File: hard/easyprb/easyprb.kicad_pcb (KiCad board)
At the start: 2 copper layers, 101 parts, among them J10 DBG, J20 RLTC, J21 CMD, J30 RS485, J40 TO EPF, J41 EPF, J50 TO RS, J51 UF RS485, Q30 S8050, Q40 2N7002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

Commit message: hardware is complete. it is does manufacture.
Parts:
- D51: value RED -> BLUE
- U30, U40, U50, U51: footprint Package_SO:SOIC-8_3.9x4.9mm_P1.27mm -> kicad_footprint_general:SOIC-8_3.9x4.9mm_P1.27mm
- U60, U61, U62, U63: footprint Package_SO:SOIC-8_5.23x5.23mm_P1.27mm -> kicad_footprint_general:SOIC-8_5.23x5.23mm_P1.27mm
- moved R32 85.3 mm to (116.8, 128.1), turned to 270 degrees
- moved R38 85.3 mm to (120.5, 137.9), turned to 90 degrees
- moved C27 80.9 mm to (112.6, 101.7), turned to 180 degrees
- moved C29 78.0 mm to (112.4, 113.7), turned to 180 degrees
- moved R30 77.4 mm to (113.3, 130.3), turned to 180 degrees
- moved J51 72.6 mm to (183.5, 136.4), turned to 90 degrees
- moved D23 72.5 mm to (116.3, 114.5), turned to 270 degrees
- moved C26 69.2 mm to (112.6, 100.2), turned to 180 degrees
- moved R21 67.6 mm to (114.7, 114.5), turned to 90 degrees
- moved C62 65.4 mm to (141.4, 135.2)
- moved J21 64.9 mm to (103.9, 110.3), turned to 90 degrees
- moved R13 64.9 mm to (127.5, 113.2)
- moved U30 64.1 mm to (121.9, 131.5), turned to 90 degrees
- moved D20 64.0 mm to (119.9, 84.5), turned to 180 degrees
- moved R34 63.8 mm to (116.8, 134.8), turned to 270 degrees
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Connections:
- J10 pad 1: /RST -> Net-(J10-Pad1)
- R37 pad 1: /LTX0 -> /LTX1
- U10 pad 11: /LE1 -> Net-(U10-Pad11)
- U10 pad 14: /LTX1 -> /EPN
- U10 pad 15: /LRX1 -> /EPN
- U10 pad 16: /TX1 -> /EPF
- U10 pad 18: /LE0 -> Net-(U10-Pad18)
- U10 pad 2: Net-(U10-Pad2) -> /TLL
- U10 pad 20: Net-(U10-Pad20) -> /TX1
- U10 pad 21: Net-(U10-Pad21) -> /LE0
- U10 pad 23: /LE2 -> Net-(U10-Pad23)
- U10 pad 24: /LTX0 -> Net-(U10-Pad24)
- U10 pad 25: /LRX0 -> Net-(U10-Pad25)
- U10 pad 26: /LRX0 -> Net-(U10-Pad26)
- U10 pad 27: /CFT -> Net-(U10-Pad27)
- U10 pad 28: Net-(U10-Pad28) -> /LEM
- U10 pad 30: Net-(U10-Pad30) -> /LRX0
- U10 pad 33: Net-(U10-Pad33) -> /LTX0
- U10 pad 34: /EPN -> Net-(U10-Pad34)
- U10 pad 35: /EPN -> /LE1
- U10 pad 36: Net-(U10-Pad36) -> /LE2
- U10 pad 37: /EPF -> /TEN
- U10 pad 38: /LE4 -> /CS3
- U10 pad 41: /LE3 -> Net-(U10-Pad41)
- U10 pad 42: /TX0 -> Net-(U10-Pad42)
- U10 pad 43: /RX0 -> Net-(U10-Pad43)
- U10 pad 44: /TLL -> Net-(U10-Pad44)
- U10 pad 46: Net-(U10-Pad46) -> /SWD
- U10 pad 47: /SWD -> /CS2
- U10 pad 48: Net-(U10-Pad48) -> /CS0
- U10 pad 51: /CS3 -> /LTX1
- U10 pad 52: /CS2 -> /LRX1
- U10 pad 53: /CS1 -> /LRX1
- U10 pad 54: /CS0 -> /CFT
- U10 pad 58: /LEM -> /CS1
- U10 pad 59: Net-(U10-Pad59) -> /LE3
- U10 pad 61: Net-(U10-Pad61) -> /TX0
- U10 pad 62: Net-(U10-Pad62) -> /RX0
- U10 pad 9: Net-(U10-Pad9) -> /LE4
- U22 pad 8: /LRX1 -> /LRX0
- U22 pad 9: /LTX1 -> /LTX0
- U30 pad 1: /LRX0 -> /LRX1
- U30 pad 4: /LTX0 -> /LTX1
- U31 pad 1: /LRX0 -> /LTX1
- U31 pad 2: /LTX0 -> /LRX1
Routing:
- net GND: track 0.00 -> 667.3 mm, vias 0 -> 85
- net VCC: track 0.00 -> 421.4 mm, vias 0 -> 23
- net /SCLK: track 0.00 -> 66.7 mm, vias 0 -> 5
- net /MOSI: track 0.00 -> 60.1 mm, vias 0 -> 4
- net /VUB: track 0.00 -> 55.8 mm, vias 0 -> 2
- net /MISO: track 0.00 -> 53.3 mm, vias 0 -> 6
- net /VUA: track 0.00 -> 46.9 mm, vias 0 -> 1
- net /LE3: track 0.00 -> 46.5 mm
- net /CS3: track 0.00 -> 43.4 mm, vias 0 -> 4
- net /LE2: track 0.00 -> 43.3 mm, vias 0 -> 2
- net /RX1: track 0.00 -> 39.1 mm
- net /LE0: track 0.00 -> 38.5 mm
- net /TX1: track 0.00 -> 38.4 mm, vias 0 -> 2
- net /TEN: track 0.00 -> 38.4 mm, vias 0 -> 2
- net /LRX1: track 0.00 -> 34.7 mm, vias 0 -> 2
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- added copper zone on B.Cu, net GND
- added copper zone on F.Cu, net GND
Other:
- board outline added: 87 x 72 mm
- net class Default: trace_width 0.25 -> 0.2; via_dia 0.8 -> 0.6
- board text added: "115200"
- board text added: "20220916_1.6_HASL"
- board text added: "A+"
- board text added: "B-"
- board text added: "CMD"
- board text added: "EASYPB_V10"
- board text added: "EPI"
- board text added: "EPO"
- board text added: "GND"
- board text added: "RIN"
- board text added: "RLTC"
- board text added: "ROT"

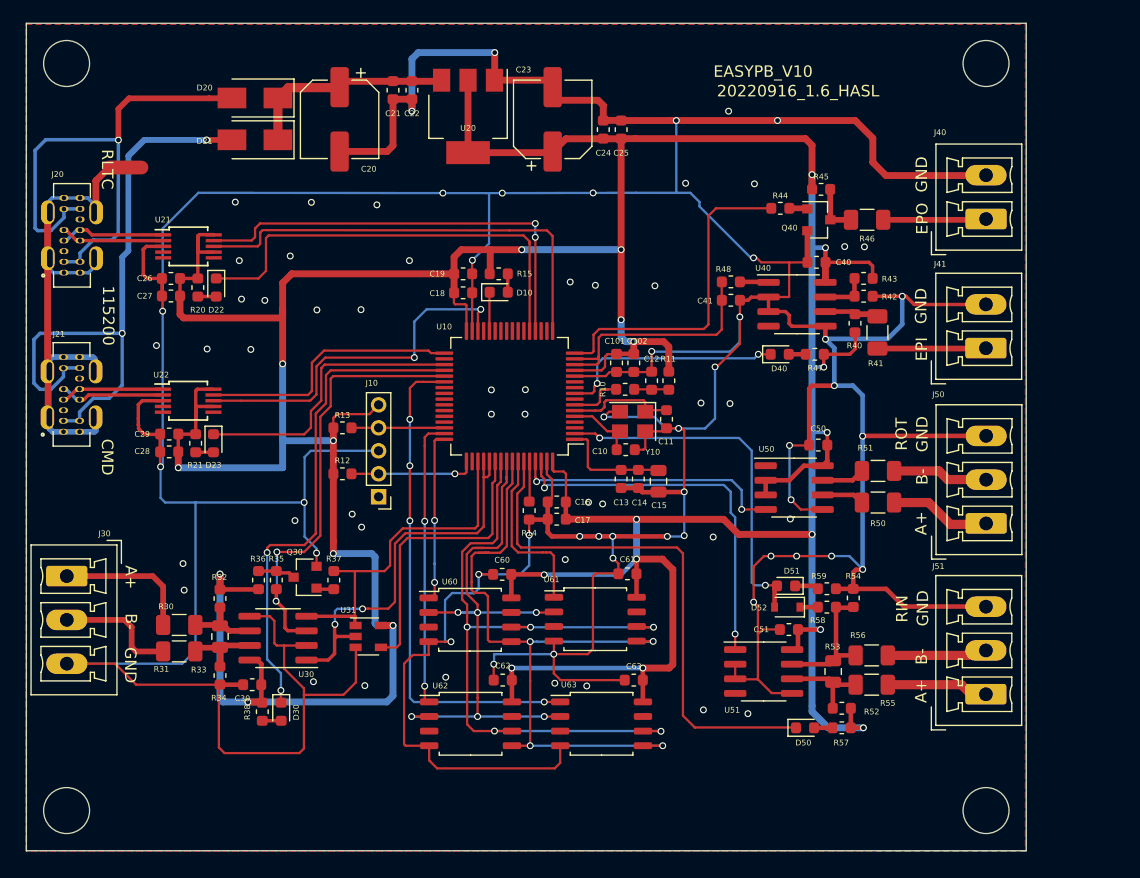
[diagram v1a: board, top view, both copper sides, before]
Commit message: 增加端子电源接口，EPF输入接口增加VCC，方便连接光电数据头
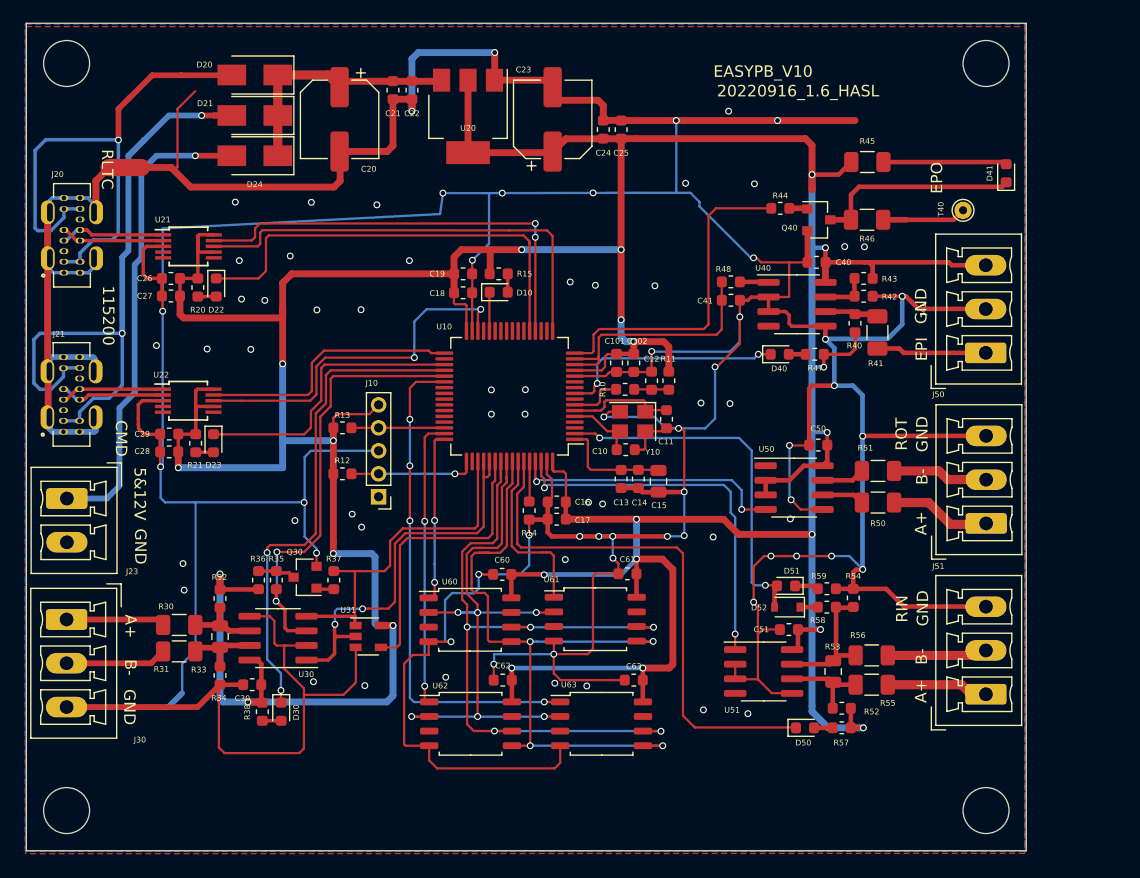
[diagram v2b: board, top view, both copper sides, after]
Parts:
- removed J40: TO EPF, kicad_footprint_general:PhoenixContact_MCV_1,5_2-G-3.81_1x02_P3.81mm_Vertical
- added D24: SS14, kicad_footprint_general:D_SMA, F.Cu at (119.9, 89.5)
- added D41: RED, kicad_footprint_general:LED_0603_1608Metric, F.Cu at (185.2, 91.0)
- added J23: PWU, kicad_footprint_general:PhoenixContact_MCV_1,5_2-G-3.81_1x02_P3.81mm_Vertical, F.Cu at (103.5, 119.3)
- added T40: TestPoint, TestPoint:TestPoint_THTPad_D1.5mm_Drill0.7mm, F.Cu at (181.5, 94.3)
- J41: footprint kicad_footprint_general:PhoenixContact_MCV_1,5_2-G-3.81_1x02_P3.81mm_Vertical -> kicad_footprint_general:PhoenixContact_MCV_1,5_3-G-3.81_1x03_P3.81mm_Vertical
- R45: value 4.7k -> 470R; footprint kicad_footprint_general:R_0603_1608Metric -> kicad_footprint_general:R_1206_3216Metric
- moved R45 4.67 mm to (173.2, 90.1)
- moved J30 3.78 mm to (103.5, 129.9)
- moved D21 2.11 mm to (119.9, 86.0)
- moved D20 2.00 mm to (119.9, 82.5)
- moved J41 0.41 mm to (183.5, 106.7)
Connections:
- Q40 pad 3: Net-(Q40-Pad3) -> Net-(D41-Pad1)
- R45 pad 2: Net-(Q40-Pad3) -> Net-(D41-Pad2)
- R46 pad 2: Net-(Q40-Pad3) -> Net-(D41-Pad1)
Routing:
- net /VUC: track 0.00 -> 41.7 mm, vias 0 -> 1
- net GND: track 667.3 -> 690.5 mm
- net Net-(D41-Pad1): track 0.00 -> 17.9 mm
- net VCC: track 421.4 -> 436.6 mm
- net Net-(D41-Pad2): track 0.00 -> 10.7 mm
- net Net-(Q40-Pad3): track 4.44 -> 0.00 mm
- net /A1: track 12.1 -> 8.60 mm
- net Net-(C20-Pad1): track 18.5 -> 22.0 mm
- net /VUB: track 55.8 -> 57.8 mm
- net /EPO: track 8.97 -> 7.29 mm
- net /B1: track 10.5 -> 9.56 mm
- net /VUA: track 46.9 -> 47.8 mm
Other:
- board text added: "5&12V"

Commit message: 修正USB封装，使焊接更加容易。
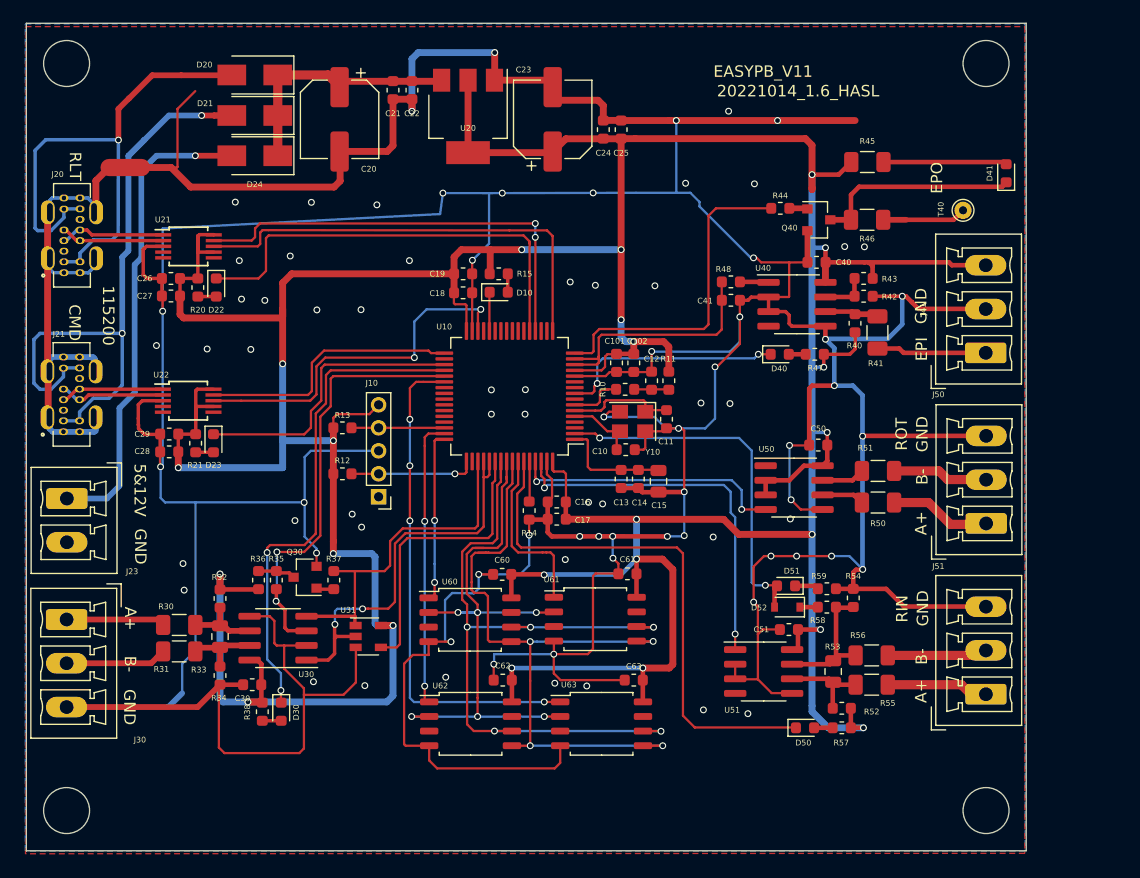
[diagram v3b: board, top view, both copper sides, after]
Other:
- board text added: "20221014_1.6_HASL"
- board text added: "EASYPB_V11"
- board text added: "RLT"
- board text removed: "20220916_1.6_HASL"
- board text removed: "EASYPB_V10"
- board text removed: "RLTC"

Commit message: modify easy prb，epo change to led type interface
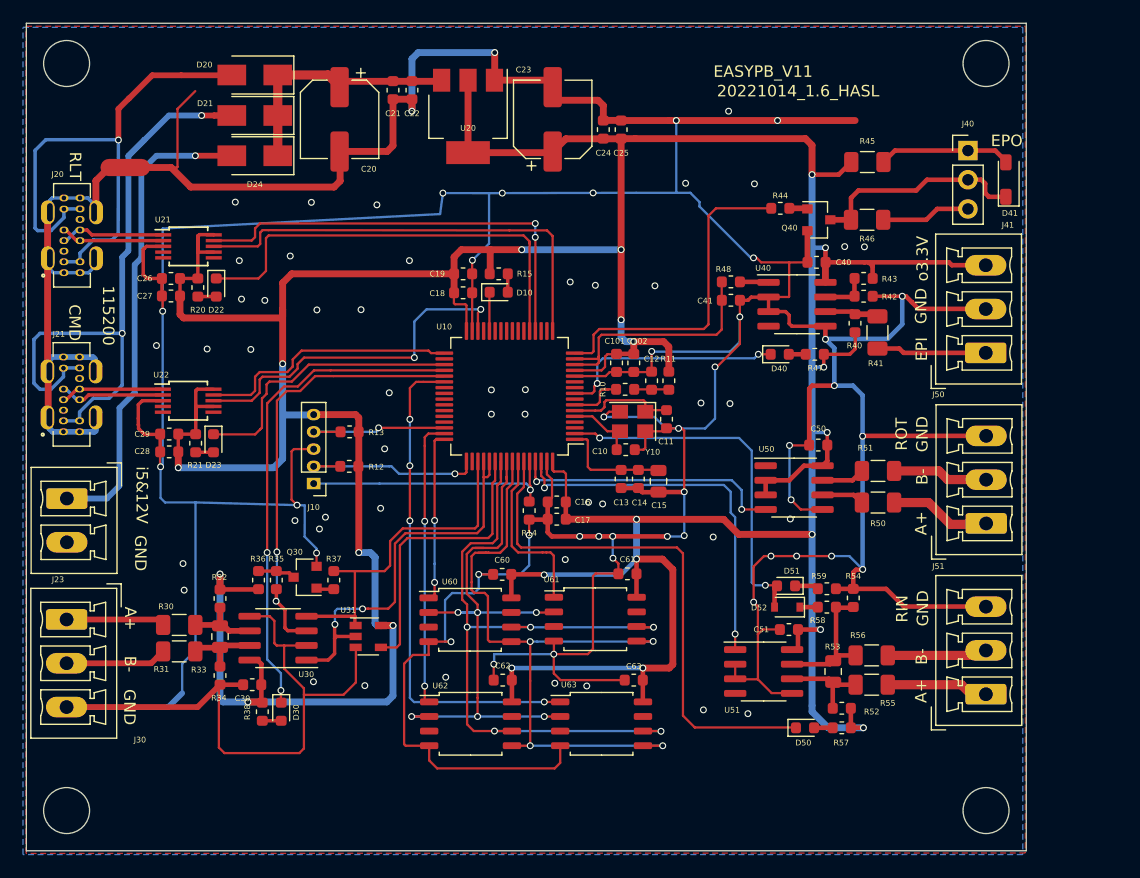
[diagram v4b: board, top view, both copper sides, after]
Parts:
- removed T40: TestPoint, TestPoint:TestPoint_THTPad_D1.5mm_Drill0.7mm
- added J40: EPO, kicad_footprint_general:PinHeader_1x03_P2.54mm_Vertical, F.Cu at (181.9, 89.1)
- D41: footprint kicad_footprint_general:LED_0603_1608Metric -> kicad_footprint_general:LED_4014
- J10: footprint kicad_footprint_general:PinHeader_1x05_P2.00mm_Vertical -> kicad_footprint_general:PinHeader_1x05_P1.50mm_Vertical
- R45: value 470R -> 180R
- moved J10 5.77 mm to (125.0, 118.0)
- moved R12 0.88 mm to (128.1, 116.5), turned to 180 degrees
- moved R13 0.72 mm to (128.1, 113.5), turned to 180 degrees
- moved D41 0.59 mm to (185.5, 91.6)
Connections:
- D41 pad 1: Net-(D41-Pad1) -> /EPO
- J10 pad 1: Net-(J10-Pad1) -> /BOOT
- Q40 pad 3: Net-(D41-Pad1) -> /EPO
- R14 pad 1: Net-(R14-Pad1) -> /BOOT
- R46 pad 1: /EPO -> Net-(J40-Pad3)
- R46 pad 2: Net-(D41-Pad1) -> /EPO
- U10 pad 60: Net-(R14-Pad1) -> /BOOT
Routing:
- net /BOOT: track 0.00 -> 22.9 mm, vias 0 -> 1
- net Net-(D41-Pad1): track 17.9 -> 0.00 mm
- net /EPO: track 7.29 -> 19.0 mm
- net Net-(J40-Pad3): track 0.00 -> 8.73 mm
- net VCC: track 436.6 -> 430.7 mm, vias 23 -> 22
- net /SWD: track 8.04 -> 13.9 mm, vias 0 -> 1
- net /SWC: track 11.0 -> 16.9 mm
- net GND: track 690.5 -> 686.5 mm, vias 85 -> 88
- net Net-(R14-Pad1): track 3.61 -> 0.00 mm
- net Net-(D41-Pad2): track 10.7 -> 11.5 mm
- net /LE1: track 25.1 -> 24.6 mm
- net /LRX0: track 31.8 -> 31.3 mm
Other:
- board text added: "i5&12V"
- board text added: "o3.3V"
- board text removed: "5&12V"

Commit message: crystal user differential pair
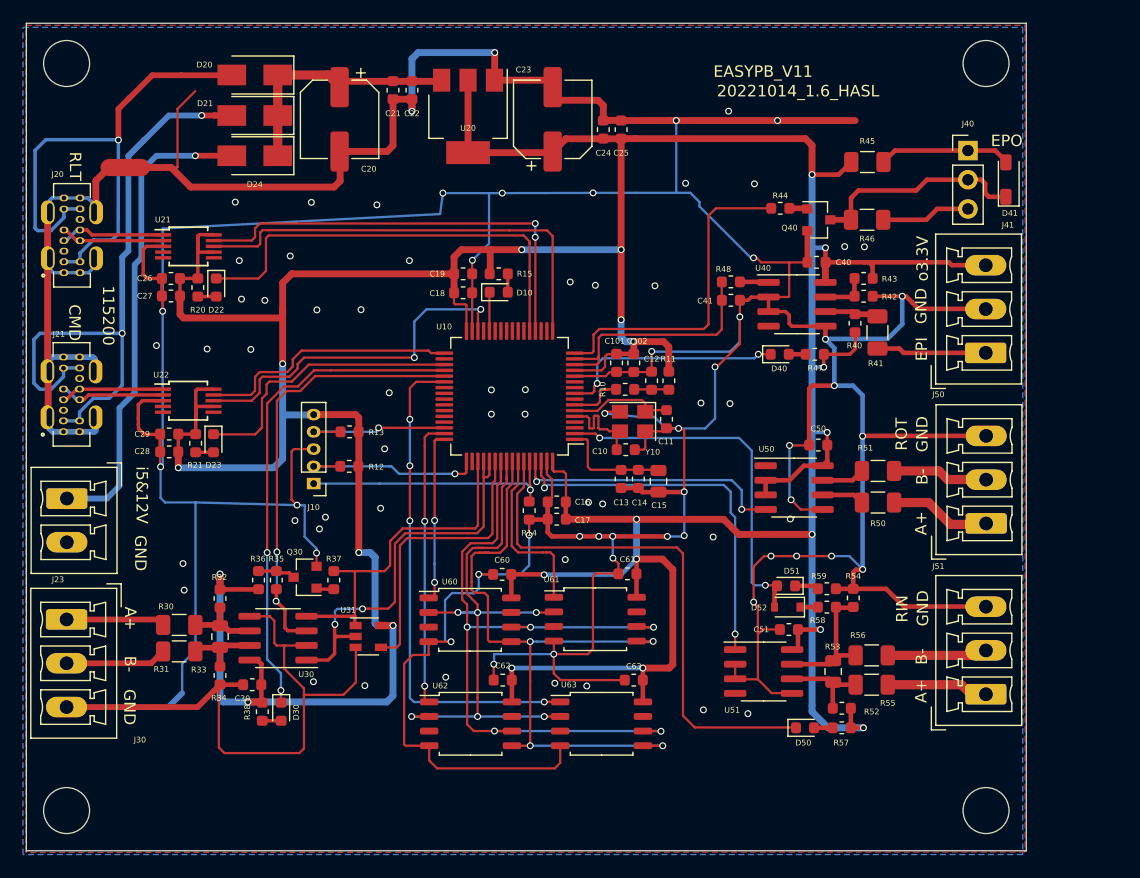
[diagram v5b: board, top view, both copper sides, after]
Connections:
- net Net-(C10-Pad1) renamed /Y_N
- net Net-(C11-Pad1) renamed /Y_P
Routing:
- net /Y_N: track 6.27 -> 8.82 mm
